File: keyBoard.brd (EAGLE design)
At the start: 60.7 x 26.4 mm, 34 parts, among them IC1 317EMP, J3 USB_A_PTH_MALE, J4 ISCP, U1 MCP73833-FCI/UN, Y2 16MHz

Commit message: routing board
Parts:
- moved J2 4.64 mm to (51.5, 26.2), turned to 180 degrees
- moved R4 4.58 mm to (30.6, 38.8)
- moved J1 4.55 mm to (25.9, 27.2)
- moved R2 3.65 mm to (29.0, 44.6), turned to 180 degrees
- moved D2 2.88 mm to (28.0, 48.7), turned to 270 degrees
- moved R6 2.02 mm to (56.5, 26.1), turned to 180 degrees
- moved R1 1.11 mm to (30.6, 46.2)
- moved R3 0.84 mm to (22.8, 48.9)
- moved C5 0.65 mm to (69.3, 36.4), turned to 180 degrees
- moved R5 0.57 mm to (30.9, 37.2)
- moved D1 0.47 mm to (30.5, 48.7), turned to 270 degrees
- moved C1 0.16 mm to (33.8, 41.5)
- turned U$3 to 0.2 degrees
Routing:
- net +3V3: track 0.00 -> 80.9 mm, vias 0 -> 3
- net D-: track 1.60 -> 23.8 mm, vias 1 -> 2
- net D+: track 1.47 -> 23.7 mm, vias 1 -> 2
- net VBAT: track 6.71 -> 28.3 mm, vias 0 -> 1
- net RESET: track 6.03 -> 26.5 mm
- net RX_FNGR: track 14.0 -> 24.5 mm
- net STAT2: track 0.00 -> 7.24 mm
- net TX_FNGR: track 16.1 -> 23.0 mm
- net VBUS: track 15.5 -> 22.3 mm
- net THERM: track 0.00 -> 5.78 mm
- net SDA: track 27.2 -> 32.8 mm
- net SCL: track 23.6 -> 28.9 mm
- net STAT1: track 0.00 -> 4.48 mm
- net N$1: track 0.00 -> 3.29 mm
- net GND: track 2.43 -> 4.56 mm, vias 0 -> 2
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
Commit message: updating board
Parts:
- added C7, C9: 1.0uF, SparkFun-Capacitors:0603
- added C8: 10uF, SparkFun-Capacitors:0603
- added D4: Yellow, SparkFun-LED:LED-0603
- added R10, R11, R15, R9: 10k, SparkFun-Resistors:0603
- added R14: 1k, SparkFun-Resistors:0603
- added R_D+, R_D-: 22, SparkFun-Resistors:0603
- added S1: (no value), SparkFun-Switches:JOYSTICK_MINI
- added U2: MCP73831, SparkFun-IC-Power:SOT23-5
- R7, R8: value 22 -> 10k
- U1: value MCP73833-FCI/UN -> MCP73833
- moved C6 108.2 mm to (-52.8, -18.9), turned to 0 degrees
- moved R8 29.8 mm to (52.7, 47.8), turned to 90 degrees
- moved R7 25.7 mm to (49.3, 47.8)
- moved R3 23.9 mm to (29.6, 25.9)
- moved C3 21.9 mm to (43.5, 27.0), turned to 90 degrees
- moved C4 21.1 mm to (35.0, 26.7), turned to 270 degrees
- moved Y2 20.6 mm to (39.6, 27.1)
- moved C5 19.7 mm to (50.7, 29.8), flipped to the top, turned to 225 degrees
- moved D3 19.2 mm to (22.5, 26.8), turned to 270 degrees
- moved C1 14.3 mm to (31.1, 27.4), flipped to the bottom
- moved IC1 11.5 mm to (27.4, 38.0), turned to 0 degrees
- moved U1 11.5 mm to (30.7, 30.3)
- moved R4 10.9 mm to (30.1, 27.9)
- moved C2 10.1 mm to (30.9, 33.0), turned to 0 degrees
- moved R5 7.95 mm to (34.8, 30.3), turned to 90 degrees
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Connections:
- new net CTR: R11.1, S1.CTR, U$1.26
- new net DOWN: R10.1, S1.D
- new net N$5: D4.C, R14.2
- new net N$6: R15.2, U2.5
- new net STAT: R14.1, U2.1
- new net UCAP: C7.1, U$1.6
- new net UP: R9.1, S1.A, U$1.27
- net +3V3: now also C9.1, R10.2, R11.2, R7.2, R8.2, R9.2; no longer U$1.6
- net D+: now also R_D+.2; no longer R7.2
- net D-: now also R_D-.2; no longer R8.2
- net GND: now also C7.2, C8.2, C9.2, R15.1, S1.GND, U2.2
- net N$2: now also R_D+.1; no longer R7.1
- net N$3: now also R_D-.1; no longer R8.1
- net SCL: now also R7.1
- net SDA: now also R8.1
- net VBAT: now also C8.1, U2.3
- net VBUS: now also D4.A, U$1.2, U2.4
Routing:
- net +3V3: track 80.9 -> 153.4 mm
- net RESET: track 26.5 -> 65.4 mm, vias 0 -> 4
- net BLE_CS: track 0.00 -> 26.5 mm, vias 1 -> 2
- net VBUS: track 22.3 -> 42.6 mm, vias 1 -> 0
- net RX_FNGR: track 24.5 -> 6.34 mm
- net TX_FNGR: track 23.0 -> 6.42 mm
- net MOSI: track 32.1 -> 48.5 mm, vias 1 -> 2
- net D+: track 23.7 -> 8.56 mm, vias 2 -> 0
- net MISO: track 28.0 -> 43.0 mm, vias 1 -> 2
- net D-: track 23.8 -> 10.0 mm
- net DOWN: track 0.00 -> 13.2 mm, vias 0 -> 1
- net CTR: track 0.00 -> 13.2 mm, vias 0 -> 1
- net UP: track 0.00 -> 12.0 mm, vias 0 -> 1
- net SCK: track 35.6 -> 46.4 mm
- net BLE_IRQ: track 29.4 -> 38.5 mm, vias 1 -> 2
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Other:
- board size 60.7 x 26.4 mm -> 61.4 x 26.6 mm

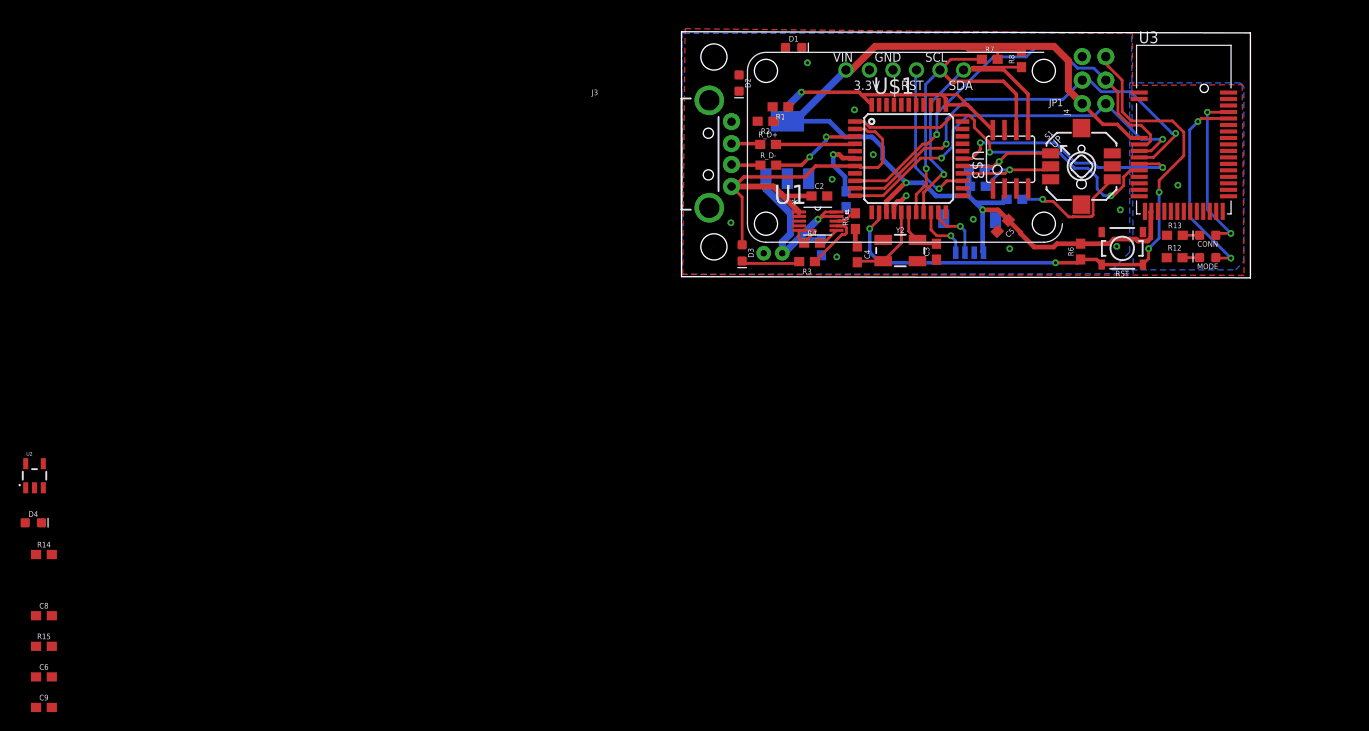
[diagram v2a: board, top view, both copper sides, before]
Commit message: editted gitignore & deleted some files
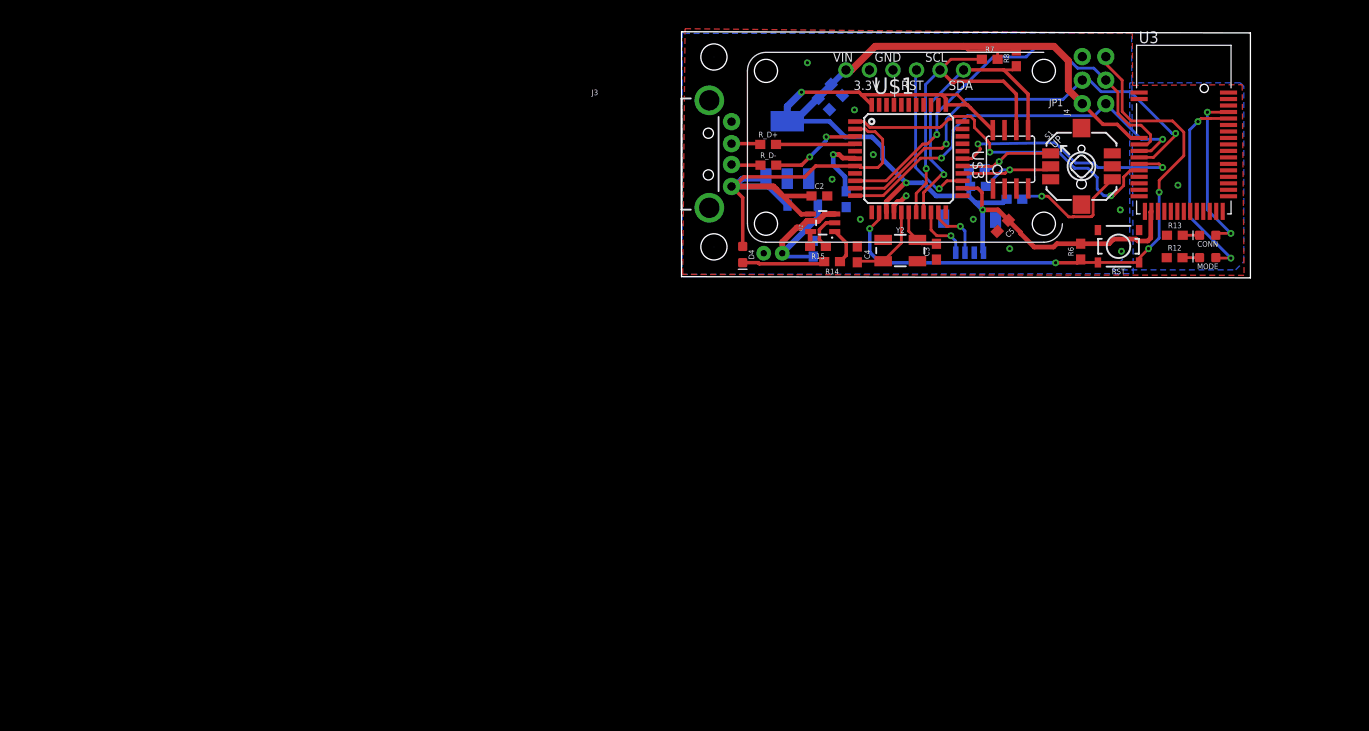
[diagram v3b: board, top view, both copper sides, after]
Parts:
- removed C1: 10uF, SparkFun-Capacitors:0603
- removed D2: Yellow, SparkFun-LED:LED-0603
- removed D3: RED, SparkFun-LED:LED-0603
- removed R1, R2, R3: 1k, SparkFun-Resistors:0603
- removed R4: 2.0k, SparkFun-Resistors:0603
- removed R5: 10k, SparkFun-Resistors:0603
- removed U1: MCP73833, Microchip-MCP73833-FCI_UN:SOP50P490X110-10N
- D1: value GREEN -> MBR120; device SparkFun-LED:LED-0603 -> adafruit:SOD-123FL
- J2: value (none) -> FINGER_SCAN
- JP1: value (none) -> SCREEN
- S1: value (none) -> JOYSTICK
- U3: value (none) -> nRF51
- moved C9 108.5 mm to (32.8, 44.5), flipped to the bottom, turned to 225 degrees
- moved C6 104.5 mm to (31.4, 42.9), flipped to the bottom, turned to 225 degrees
- moved R15 94.1 mm to (30.7, 27.6), turned to 180 degrees
- moved C8 92.0 mm to (30.2, 27.3), flipped to the bottom, turned to 90 degrees
- moved R14 90.8 mm to (32.3, 25.9), turned to 180 degrees
- moved U2 89.4 mm to (31.2, 30.1), turned to 90 degrees
- moved D4 81.9 mm to (22.6, 26.7), turned to 270 degrees
- moved D1 17.0 mm to (29.1, 32.0), flipped to the bottom, turned to 180 degrees
- moved R8 0.57 mm to (52.1, 47.9)
- moved RST 0.47 mm to (63.2, 27.6)
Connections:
- removed net N$1: D2.C, R2.2
- removed net N$4: D1.C, R1.2
- removed net N$7: D3.C, R3.2
- removed net PG: R3.1, U1.7
- removed net PROG: R4.2, U1.6
- removed net STAT1: R2.1, U1.3
- removed net STAT2: R1.1, U1.4
- removed net THERM: R5.2, U1.8
- net GND: no longer C1.2, R4.1, R5.1, U1.5
- net VBAT: now also D1.A; no longer C1.1, IC1.3, U1.10, U1.9
- net VBUS: now also D1.C, IC1.3; no longer D1.A, D2.A, D3.A, U1.1, U1.2
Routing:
- net VBUS: track 42.6 -> 56.2 mm
- net +3V3: track 153.4 -> 164.9 mm
- net N$5: track 0.00 -> 8.95 mm
- net PG: track 6.41 -> 0.00 mm
- net N$7: track 6.33 -> 0.00 mm
- net VBAT: track 23.6 -> 18.4 mm, vias 1 -> 0
- net SDA: track 36.1 -> 31.9 mm
- net STAT: track 0.00 -> 4.05 mm
- net GND: track 9.75 -> 6.86 mm, vias 12 -> 11
- net THERM: track 2.38 -> 0.00 mm
- net PROG: track 2.32 -> 0.00 mm
- net N$6: track 0.00 -> 1.61 mm
- net RESET: track 65.4 -> 64.9 mm

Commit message: forgot to connect DOWN on the joystick
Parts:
- moved D1 2.57 mm to (31.6, 32.0)
- moved C7 1.86 mm to (35.6, 33.1)
- moved C6 0.47 mm to (31.7, 43.3)
- moved C9 0.29 mm to (33.0, 44.6)
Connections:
- net DOWN: now also U$1.22
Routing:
- net DOWN: track 13.5 -> 29.1 mm, vias 1 -> 3
- net VBUS: track 56.2 -> 60.4 mm
- net VBAT: track 18.4 -> 20.2 mm
- net UCAP: track 7.08 -> 7.86 mm
- net +3V3: track 164.9 -> 165.4 mm
- net GND: vias 11 -> 10

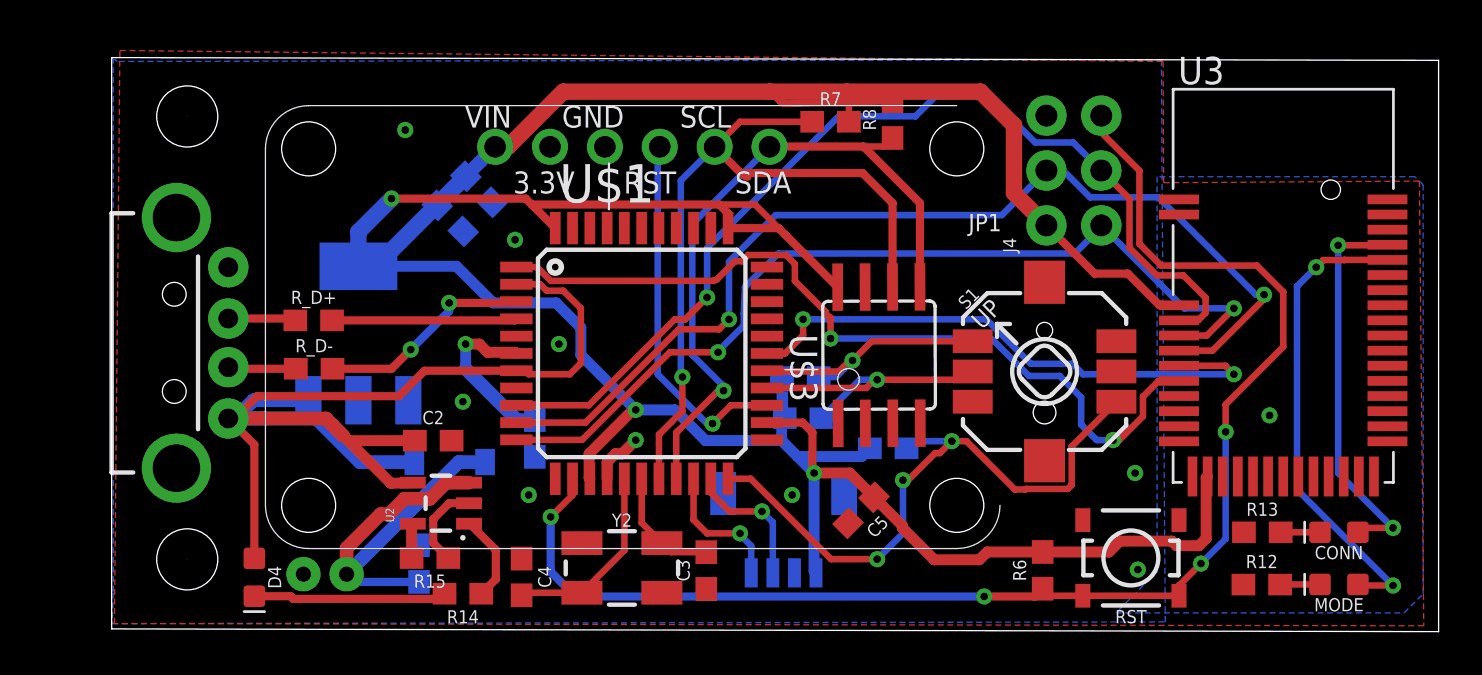
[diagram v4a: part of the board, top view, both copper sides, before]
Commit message: final board, mid-semester arduino proof of concept, non-working disjoint AVR C code
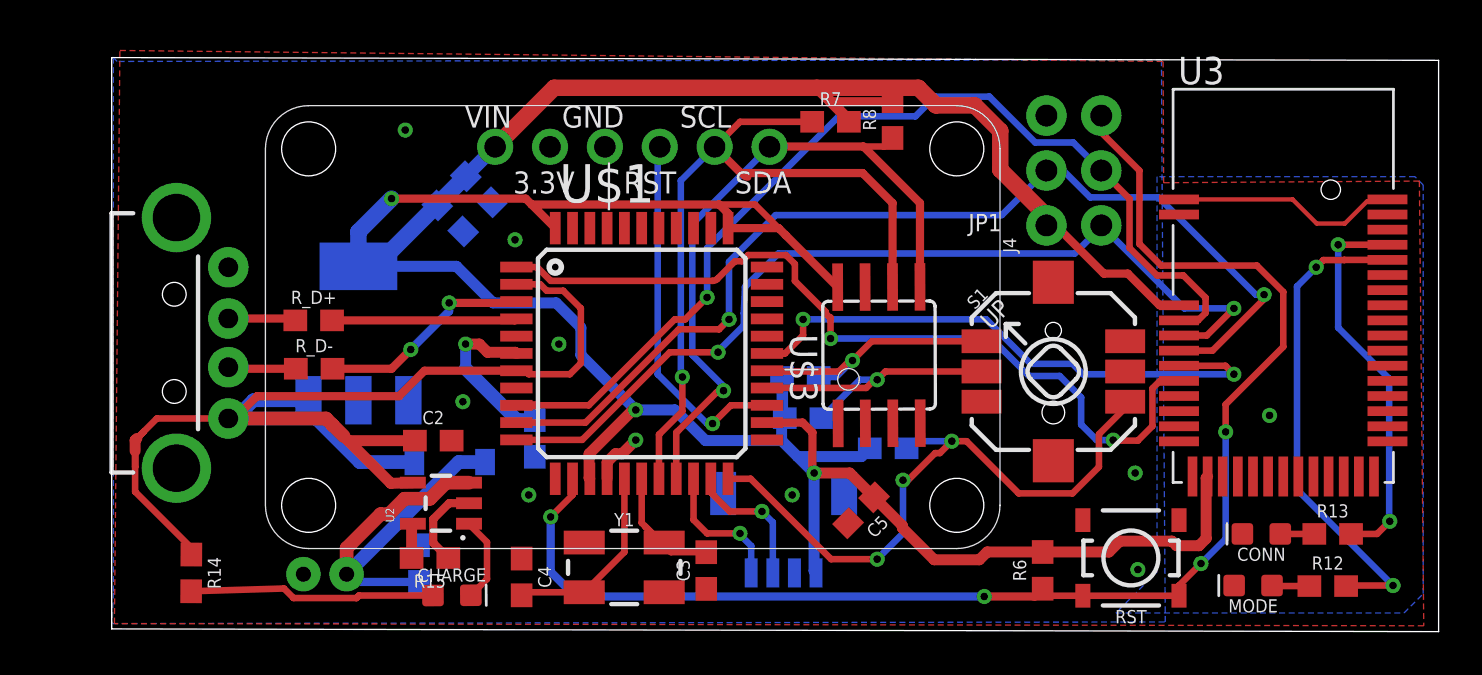
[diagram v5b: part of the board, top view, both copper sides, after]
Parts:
- removed D4: Yellow, SparkFun-LED:LED-0603
- removed Y2: 16MHz, SparkFun-Clocks:CRYSTAL-SMD-5X3.2-4PAD
- added CHARGE: Yellow, SparkFun-LED:LED-0603
- added Y1: 8MHz, SparkFun-Clocks:CRYSTAL-SMD-5X3.2-4PAD
- moved R14 12.6 mm to (19.7, 26.9), turned to 269.7 degrees
- moved MODE 3.97 mm to (68.8, 26.3)
- moved CONN 3.59 mm to (69.2, 28.7)
- moved R13 3.26 mm to (72.5, 28.7)
- moved R12 3.05 mm to (72.3, 26.3)
- moved S1 0.41 mm to (59.6, 36.2)
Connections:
- removed net CONNECTED: CONN.A, U3.39
- removed net N$10: MODE.C, R12.2
- removed net N$13: CONN.C, R13.2
- removed net N$5: D4.C, R14.2
- new net CONNECTION: R13.2, U3.39
- new net N$1: CHARGE.A, R14.2
- new net N$4: MODE.A, R12.1
- new net N$7: CONN.A, R13.1
- net GND: now also CONN.C, MODE.C; no longer R12.1, R13.1
- net MODE: now also R12.2; no longer MODE.A
- net STAT: now also CHARGE.C; no longer R14.1
- net VBUS: now also R14.1; no longer D4.A
- net XTAL1: now also Y1.3; no longer Y2.3
- net XTAL2: now also Y1.1; no longer Y2.1
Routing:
- net CONNECTED: track 18.1 -> 0.00 mm, vias 2 -> 0
- net CONNECTION: track 0.00 -> 18.1 mm, vias 0 -> 2
- net N$1: track 0.00 -> 11.6 mm
- net GND: track 6.86 -> 17.4 mm
- net N$5: track 8.95 -> 0.00 mm
- net VBUS: track 60.4 -> 64.8 mm
- net N$10: track 1.85 -> 0.00 mm
- net N$13: track 1.82 -> 0.00 mm
- net N$4: track 0.00 -> 1.74 mm
- net N$7: track 0.00 -> 1.58 mm
- net XTAL1: track 5.87 -> 6.77 mm
- net +3V3: track 165.4 -> 164.7 mm
- net DOWN: track 29.1 -> 29.7 mm
- net MODE: track 22.0 -> 22.6 mm
- net BLE_IRQ: track 38.4 -> 38.9 mm
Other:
- outline, holes or cut-outs redrawn
- board text added: "Tyler Goulding"
- board text removed: "Tyler Goulding & Fatema Almeshqab"
